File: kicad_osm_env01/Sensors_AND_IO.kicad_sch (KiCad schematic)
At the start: 40 parts, among them J1 STX-3000, J3 STX-3000, J8 Conn_01x06, J9 STX-3000, U10 ICS-43434, U12 MIC94073YC6, U3 VEML7700-TT

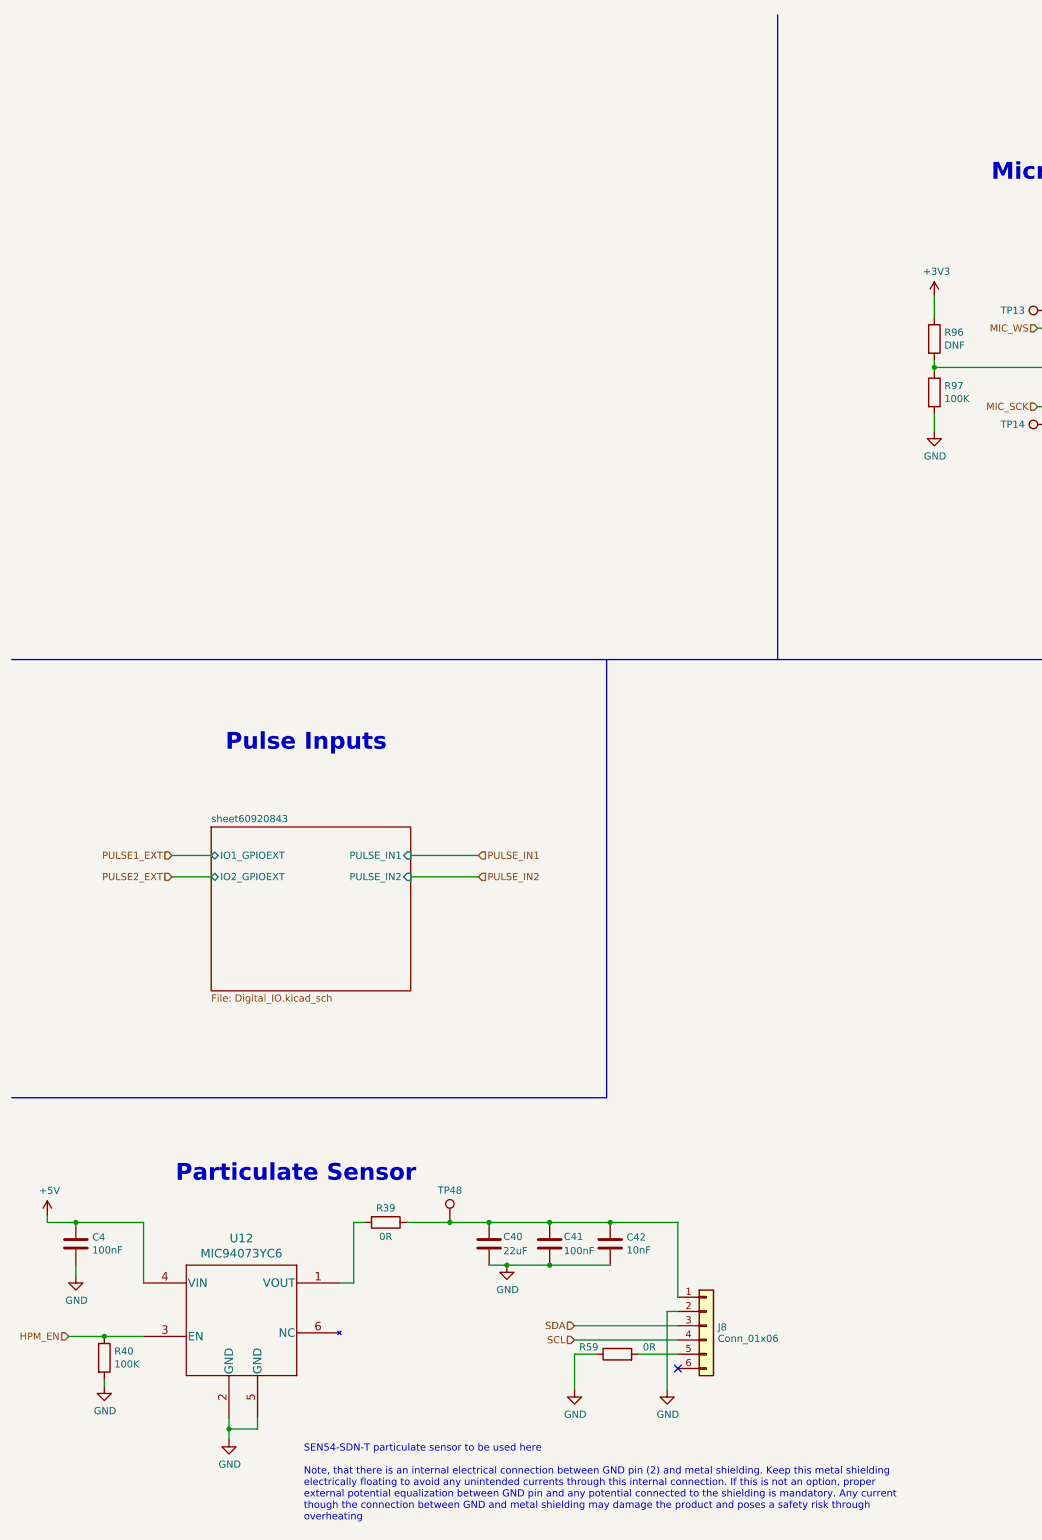
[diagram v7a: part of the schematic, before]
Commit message: updated pulse circuit for 3.3v-24v input and started layout updates
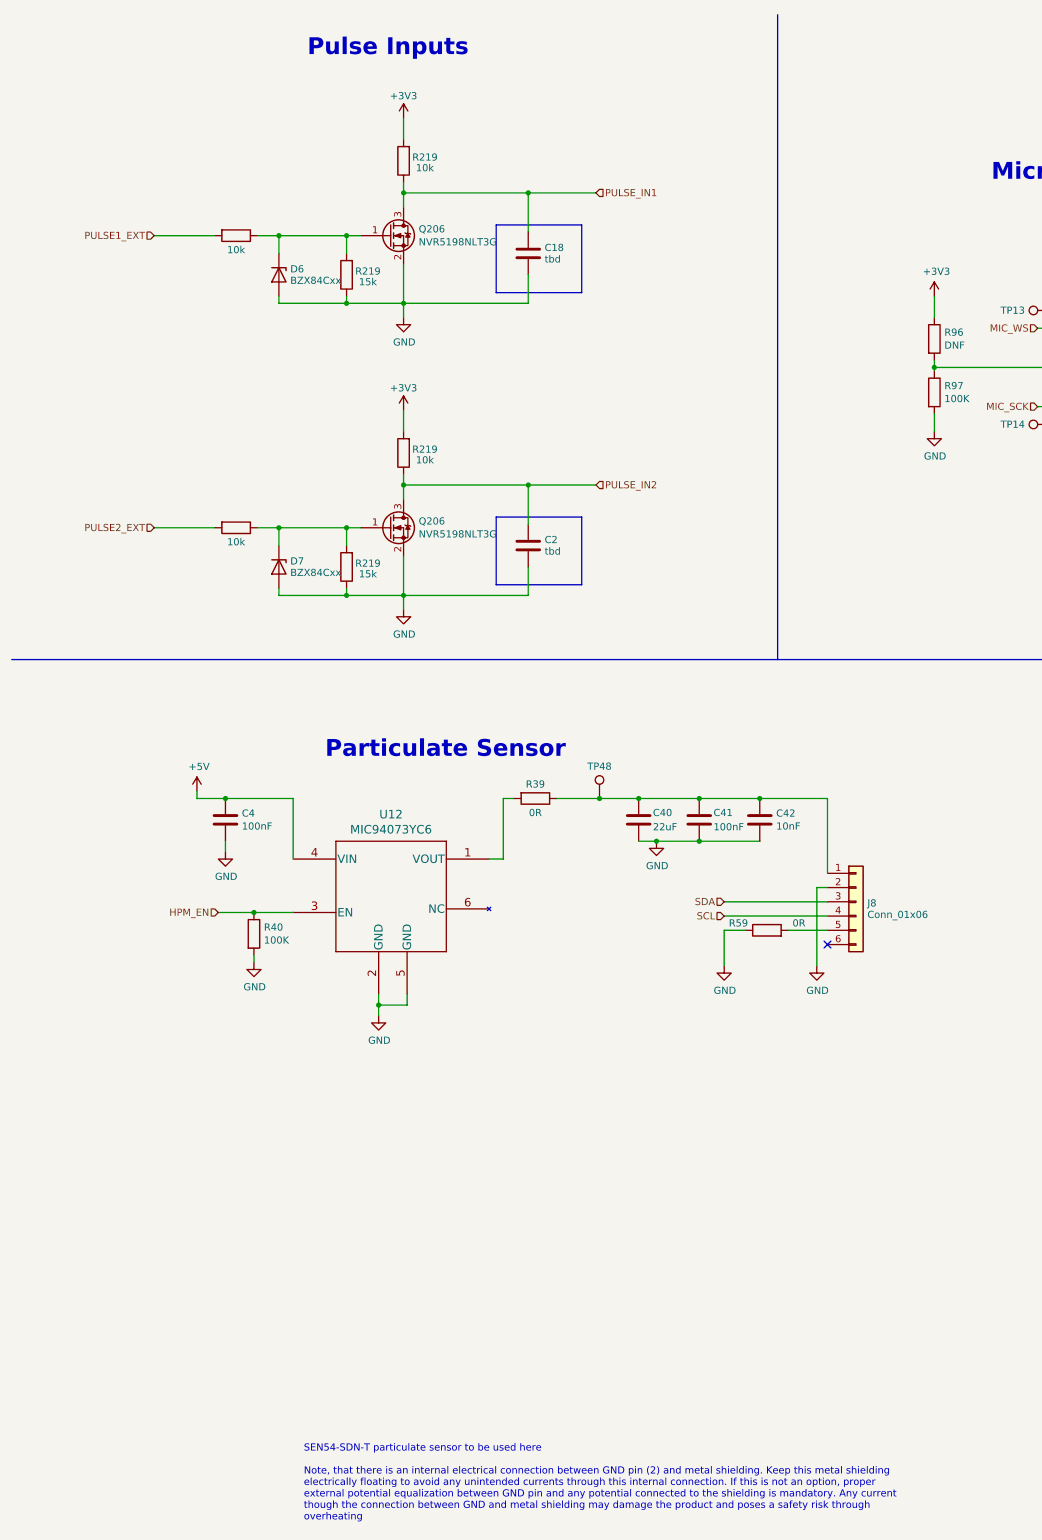
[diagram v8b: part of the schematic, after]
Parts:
- added C18, C2: tbd, Capacitor_SMD:C_0603_1608Metric, symbol Device:C
- added D6, D7: BZX84Cxx, Package_TO_SOT_SMD:SOT-23, symbol Diode:BZX84Cxx
- added Q206 (x2): NVR5198NLT3G, Package_TO_SOT_SMD:SOT-23, symbol LoTI_Board-rescue:Q_NMOS_GSD-device
- added R218 (x2): 10k, Resistor_SMD:R_0805_2012Metric, symbol LoTI_Board-rescue:R-device
- added R219 (x2): 15k, Resistor_SMD:R_0603_1608Metric, symbol LoTI_Board-rescue:R-device
- added R219 (x2): 10k, Resistor_SMD:R_0603_1608Metric, symbol LoTI_Board-rescue:R-device
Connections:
- net +3V3: now also R219.2, R219.2
- net GND: now also C18.2, C2.2, D6.1 (A), D7.1 (A), Q206.2 (S), Q206.2 (S), R219.1, R219.1
- net PULSE1_EXT: now also R218.2
- net PULSE2_EXT: now also R218.2
- net PULSE_IN1: now also C18.1, Q206.3 (D), R219.1
- net PULSE_IN2: now also C2.1, Q206.3 (D), R219.1
- new net: D6.3 (K), Q206.1 (G), R218.1, R219.2
- new net: D7.3 (K), Q206.1 (G), R218.1, R219.2
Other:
- removed sheet sheet60920843
- moved on the sheet: C4, C40, C41, C42, J8, R39, R40, R59, TP48, U12
